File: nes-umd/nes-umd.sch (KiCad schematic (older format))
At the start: 2 parts, among them CON101 NES-CONN, CON102 UMD-CONN

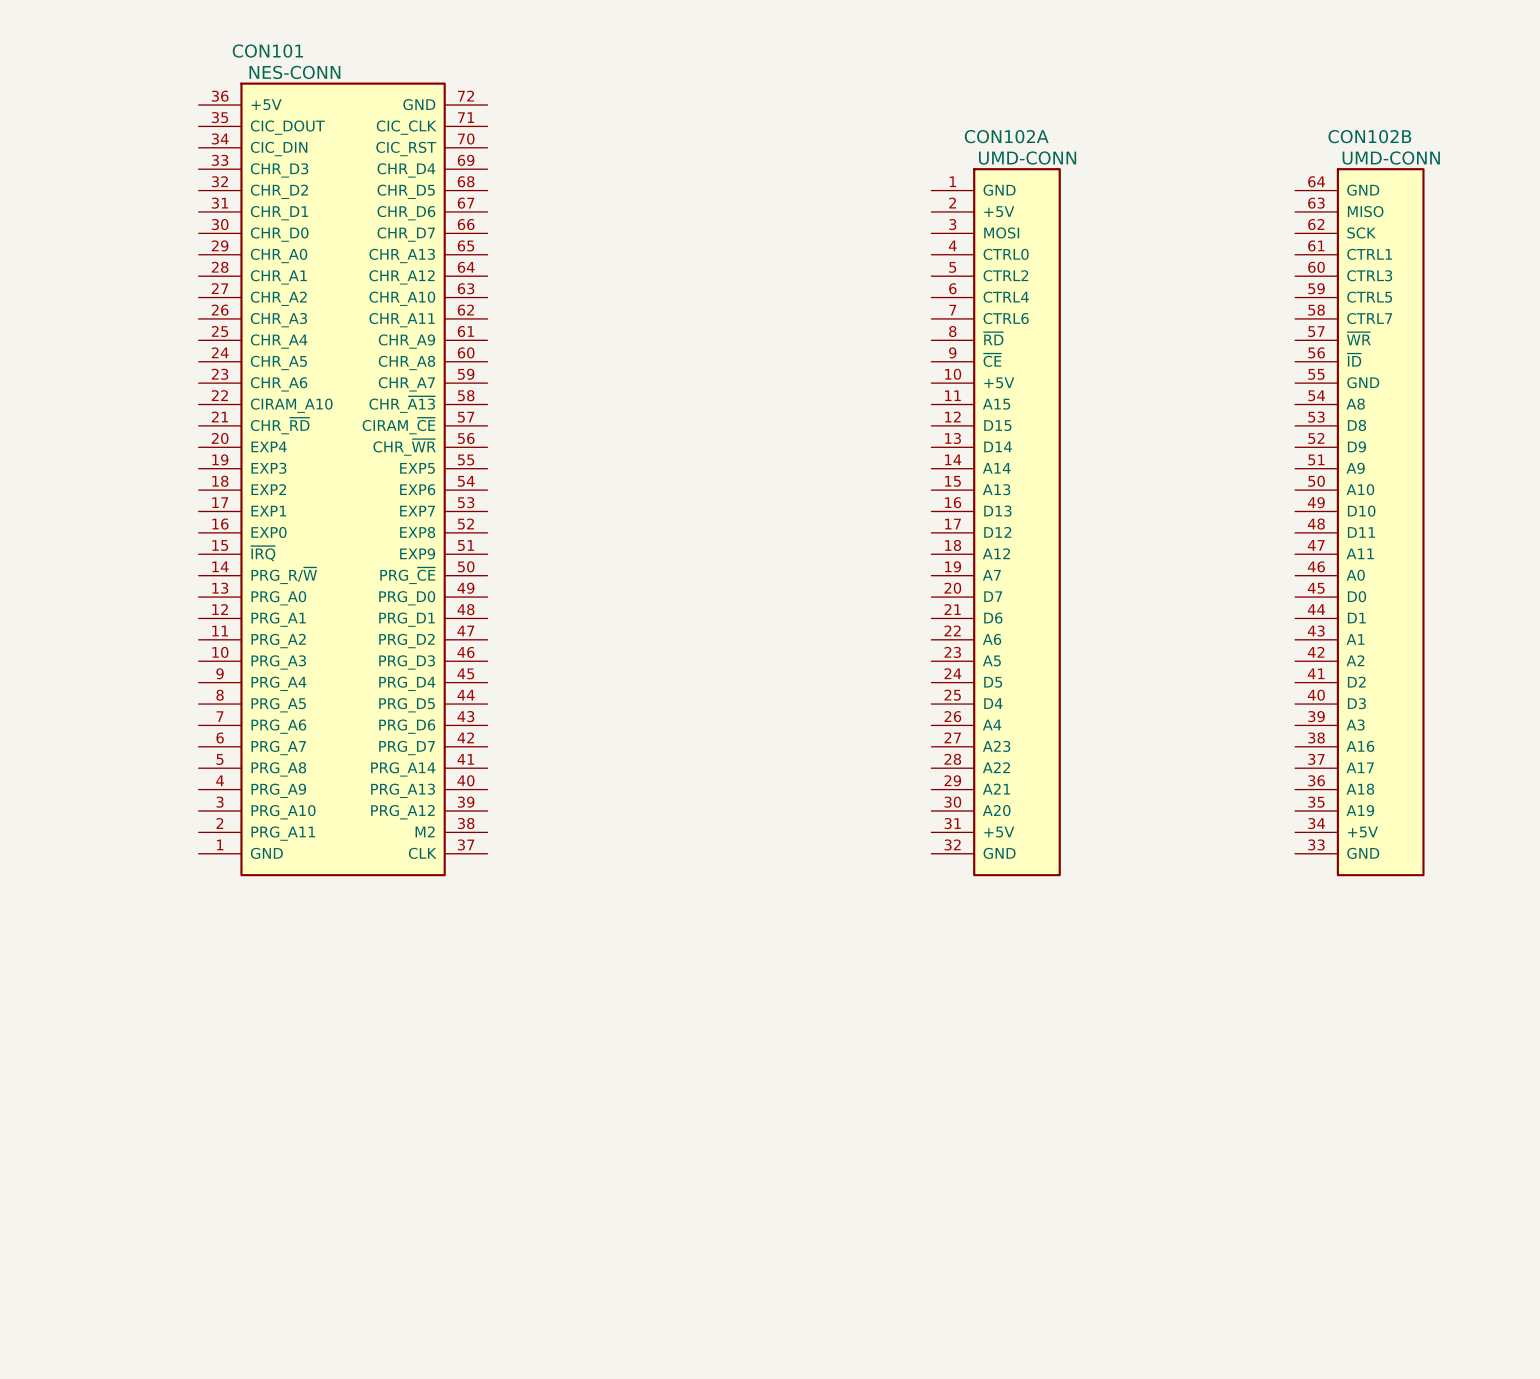
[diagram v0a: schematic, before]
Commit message: added a few net labels
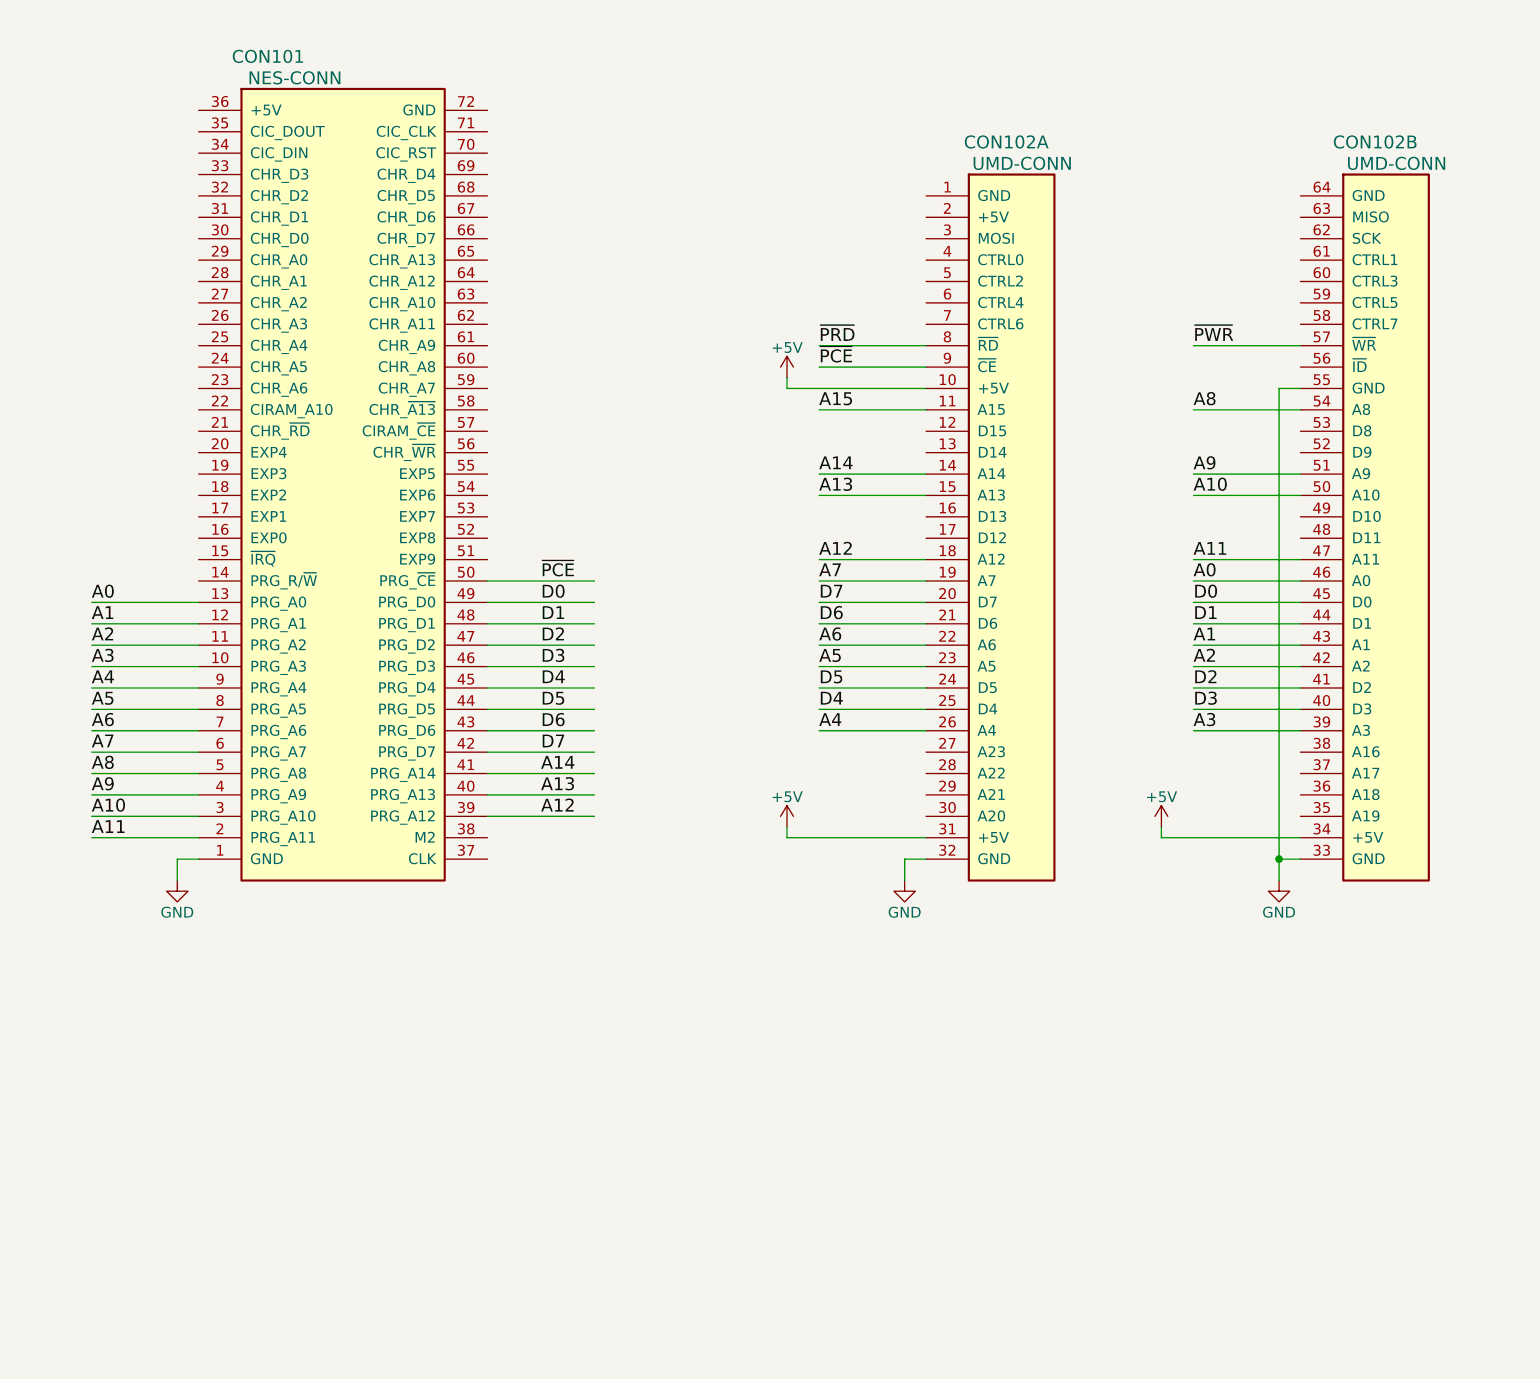
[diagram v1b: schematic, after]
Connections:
- net labels added: +5V, A0, A1, A10, A11, A12, A13, A14, A15, A2, A3, A4, A5, A6, A7, A8, A9, D0, D1, D2, D3, D4, D5, D6, D7, GND, ~PCE, ~PRD, ~PWR
- wire segments 0 -> 64
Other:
- moved on the sheet: CON101, CON102A, CON102B

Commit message: schematic work
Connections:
- net labels added: CA10, CA13, ~A13, ~CICE, ~CRD, ~CWR, ~IRQ
- wire segments 64 -> 97
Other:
- moved on the sheet: CON101, CON102A, CON102B

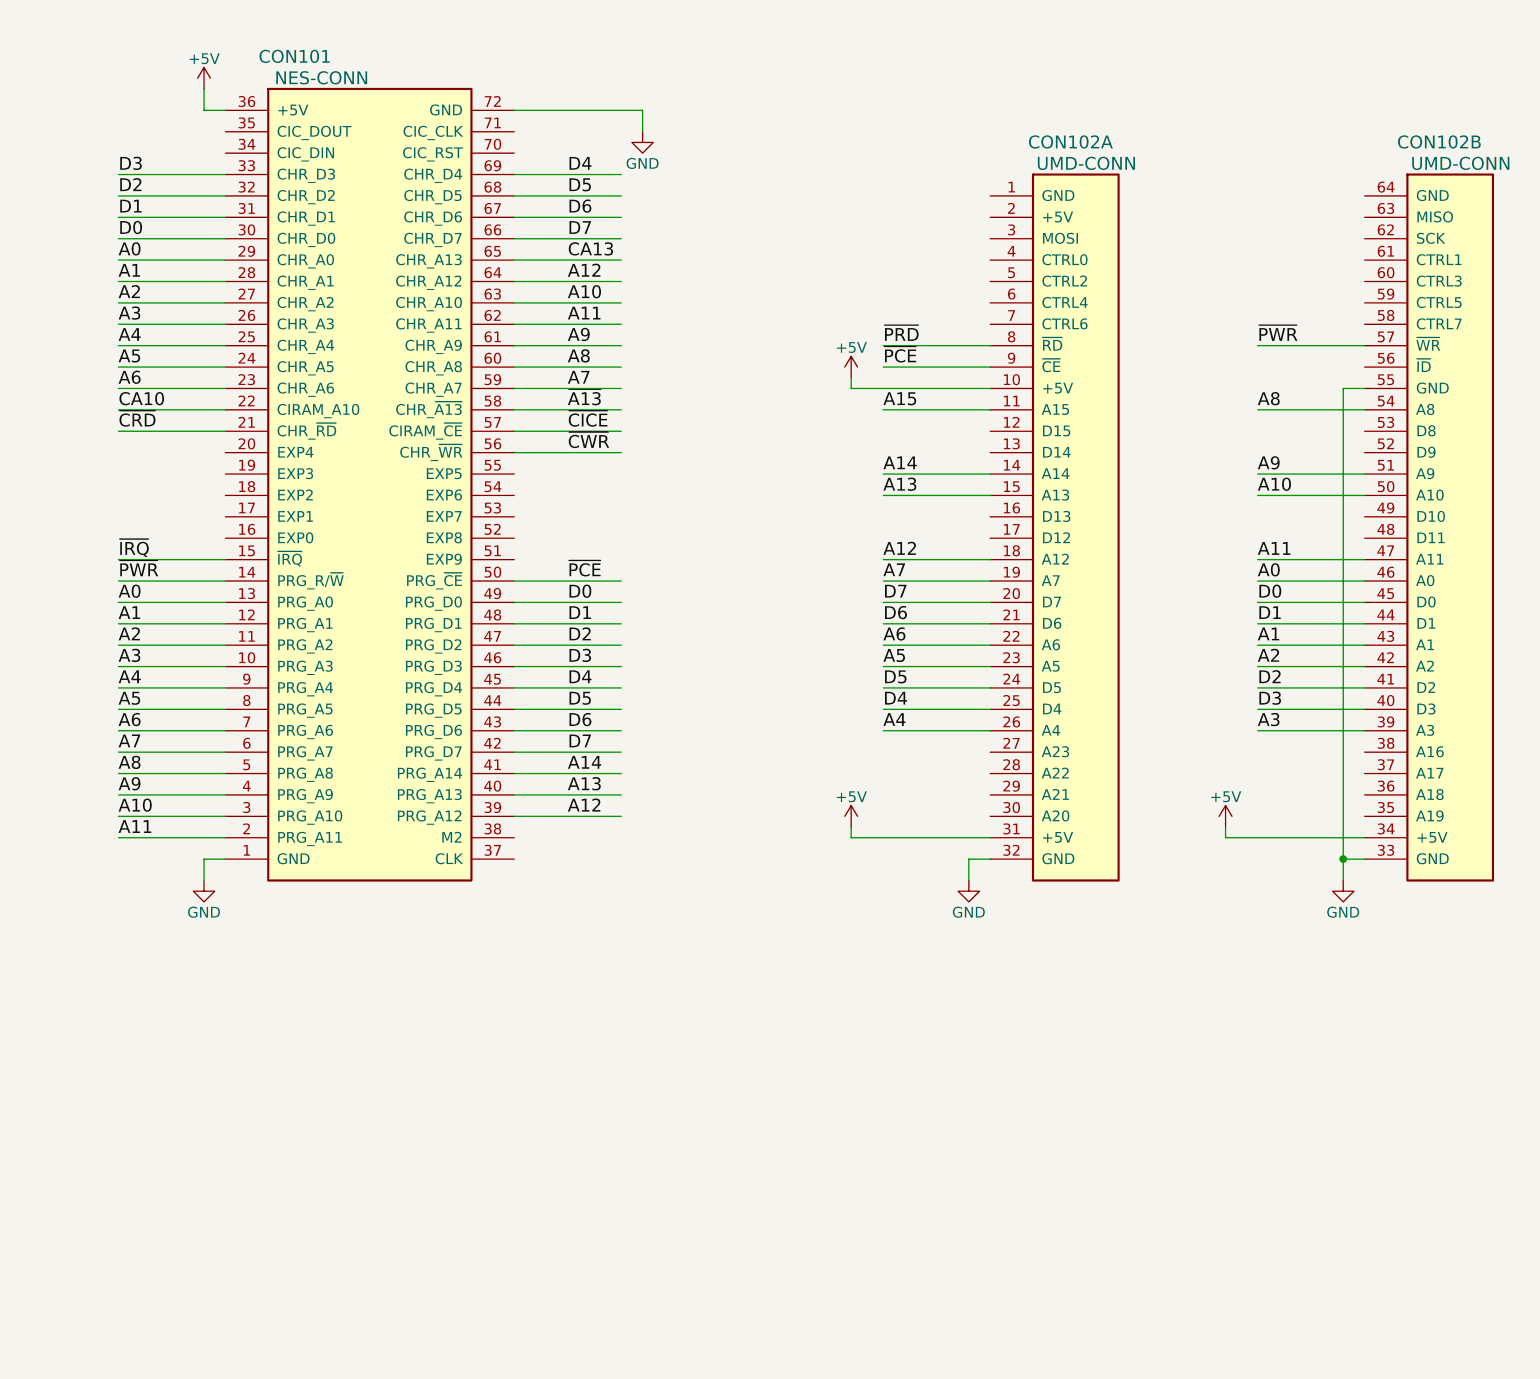
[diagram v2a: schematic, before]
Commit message: adding shift register ID to schematic
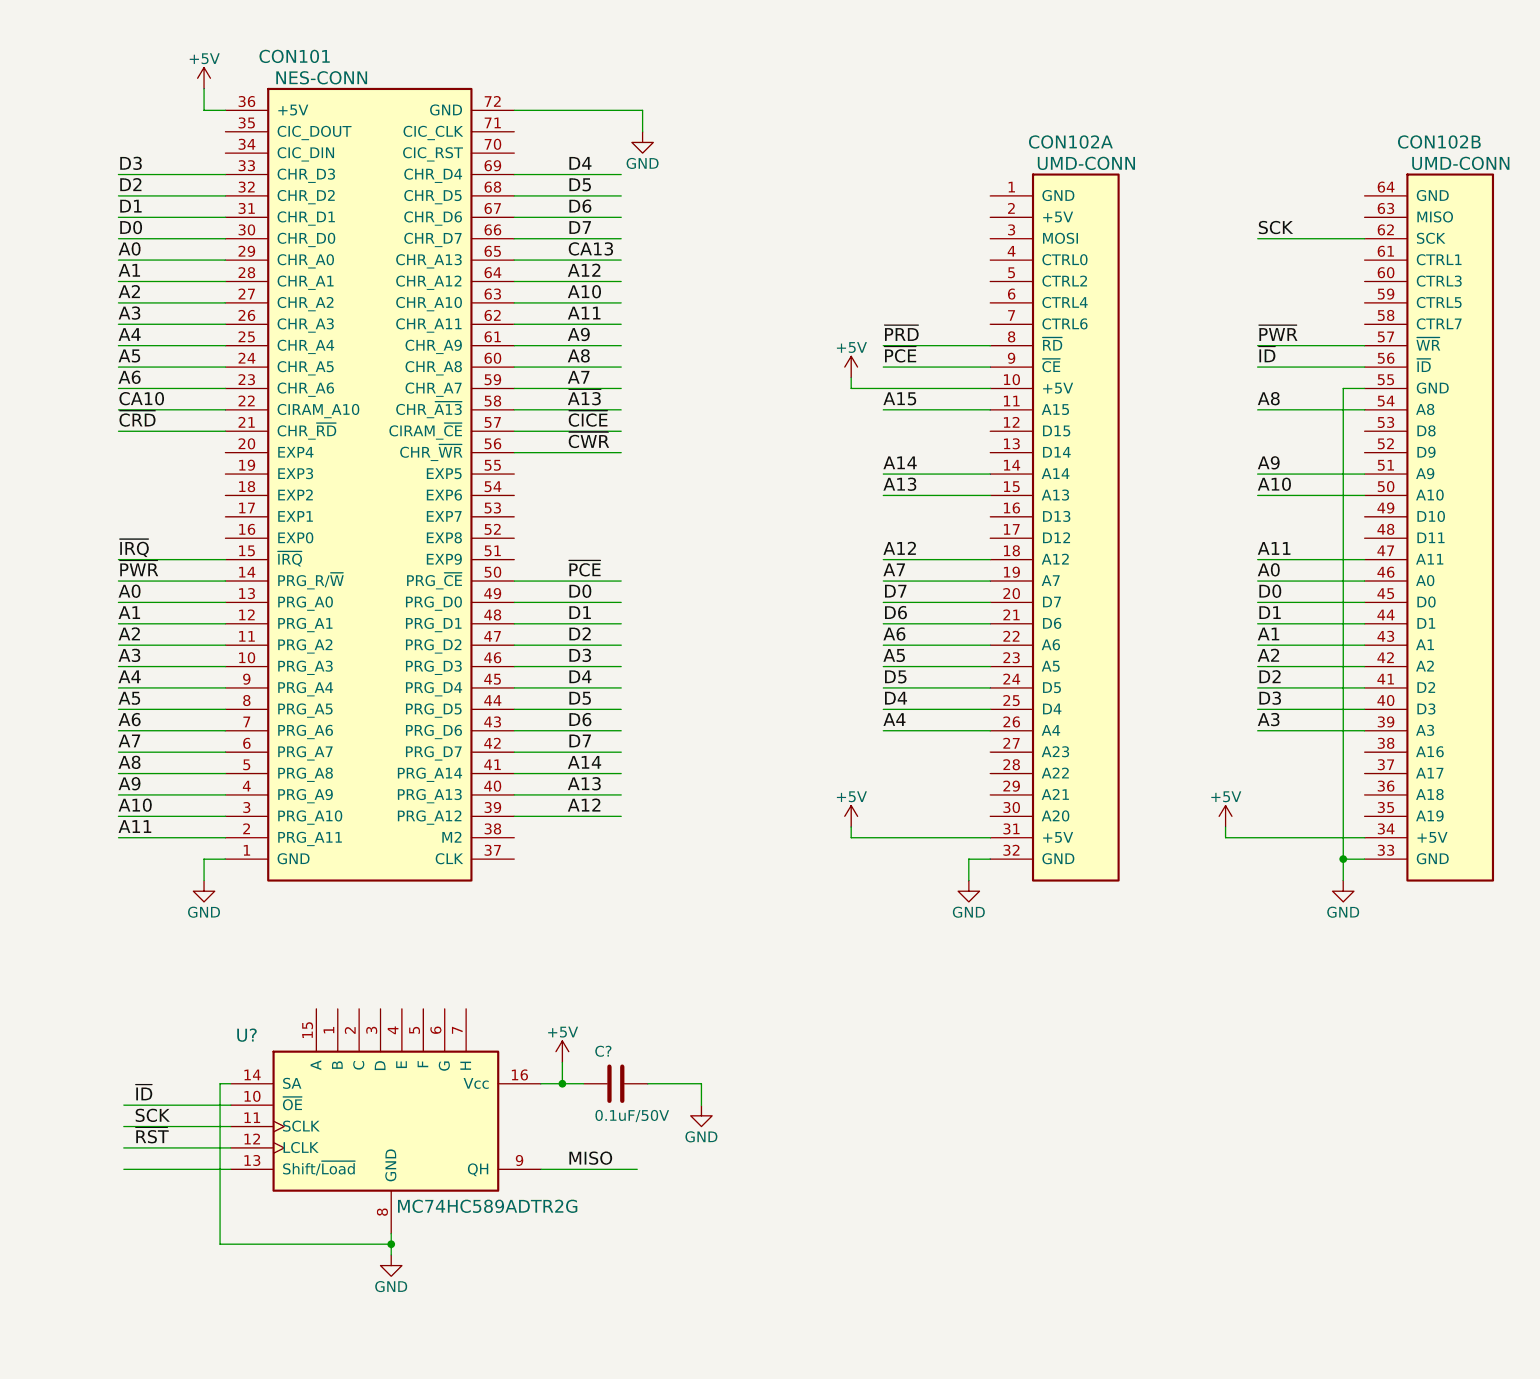
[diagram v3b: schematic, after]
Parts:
- added C?: 0.1uF/50V, db-smt:0603, symbol C_0603
- added U?: MC74HC589ADTR2G, db-smt:TSSOP-16, symbol MC74HC589ADTR2G
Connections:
- net labels added: MISO, SCK, ~ID, ~RST
- wire segments 97 -> 112
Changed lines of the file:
@@
 EndData
 $EndBitmap
+$Comp
+L MC74HC589ADTR2G U?
+U 1 1 5AB17DEA
+P 2950 6300
+F 0 "U?" H 2825 6375 60  0000 C CNN
+F 1 "MC74HC589ADTR2G" H 3950 5575 60  0000 C CNN
+F 2 "db-smt:TSSOP-16" H 3425 7000 60  0001 C CNN
+F 3 "http://www.onsemi.com/pub/Collateral/MC74HC589A-D.PDF" H 4400 6900 60  0001 C CNN
+F 4 "MC74HC589ADTR2GOSCT-ND" H 3650 6800 60  0001 C CNN "Digikey"
+F 5 "IC SHIFT REGISTER 8BIT 16-TSSOP" H 3800 6700 60  0001 C CNN "Description"
+	1    2950 6300
+	1    0    0    -1
+$EndComp
+$Comp
+L GND #PWR?
+U 1 1 5AB17ED4
+P 3500 7250
+F 0 "#PWR?" H 3500 7000 50  0001 C CNN
+F 1 "GND" H 3500 7100 50  0000 C CNN
+F 2 "" H 3500 7250 50  0001 C CNN
+F 3 "" H 3500 7250 50  0001 C CNN
+	1    3500 7250
+	1    0    0    -1
+$EndComp
+Wire Wire Line
+	3500 7150 3500 7250
+Wire Wire Line
+	4200 6850 4650 6850
+Text Label 4325 6850 0    60   ~ 0
+MISO
+Wire Wire Line
+	2750 6650 2250 6650
+Wire Wire Line
+	2250 6550 2750 6550
+Wire Wire Line
+	2750 6750 2250 6750
+Wire Wire Line
+	2750 6850 2250 6850
+Wire Wire Line
+	2750 6450 2700 6450
+Wire Wire Line
+	2700 6450 2700 7200
+Wire Wire Line
+	2700 7200 3500 7200
+Connection ~ 3500 7200
+Text Label 2300 6550 0    60   ~ 0
+~ID
+Text Label 2300 6650 0    60   ~ 0
+SCK
+Text Label 2300 6750 0    60   ~ 0
+~RST
+$Comp
+L +5V #PWR?
+U 1 1 5AB199F3
+P 4300 6350
+F 0 "#PWR?" H 4300 6200 50  0001 C CNN
+F 1 "+5V" H 4300 6490 50  0000 C CNN
+F 2 "" H 4300 6350 50  0001 C CNN
+F 3 "" H 4300 6350 50  0001 C CNN
+	1    4300 6350
+	1    0    0    -1
+$EndComp
+$Comp
+L C_0603 C?
+U 1 1 5AB1A108
+P 4550 6450
+F 0 "C?" V 4400 6350 50  0000 L CNN
+F 1 "0.1uF/50V" V 4700 6350 50  0000 L CNN
+F 2 "db-smt:0603" H 5050 6350 30  0001 C CNN
+F 3 "" H 4575 6550 60  0001 C CNN
+F 4 "#ND" H 4975 6425 60  0001 C CNN "Digikey"
+F 5 "#ND" H 4975 6525 60  0001 C CNN "Description"
+	1    4550 6450
+	0    1    1    0
+$EndComp
+$Comp
+L GND #PWR?
+U 1 1 5AB1A4A7
+P 4950 6550
+F 0 "#PWR?" H 4950 6300 50  0001 C CNN
+F 1 "GND" H 4950 6400 50  0000 C CNN
+F 2 "" H 4950 6550 50  0001 C CNN
+F 3 "" H 4950 6550 50  0001 C CNN
+	1    4950 6550
+	1    0    0    -1
+$EndComp
+Wire Wire Line
+	4400 6450 4200 6450
+Wire Wire Line
+	4300 6350 4300 6450
+Connection ~ 4300 6450
+Wire Wire Line
+	4700 6450 4950 6450
+Wire Wire Line
+	4950 6450 4950 6550
+Wire Wire Line
+	8050 3100 7550 3100
+Text Label 7550 3100 0    60   ~ 0
+~ID
+Wire Wire Line
+	8050 2500 7550 2500
+Text Label 7550 2500 0    60   ~ 0
+SCK
 $EndSCHEMATC
